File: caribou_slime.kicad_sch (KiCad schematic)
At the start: 30 parts, among them J1 BATT JST, Q1 AO3145, U1 ESP32-C3_SUPERMINI, U2 BMI270, U4 ME6211C33M5G, U5 FS312F-G, U6 FS8205A

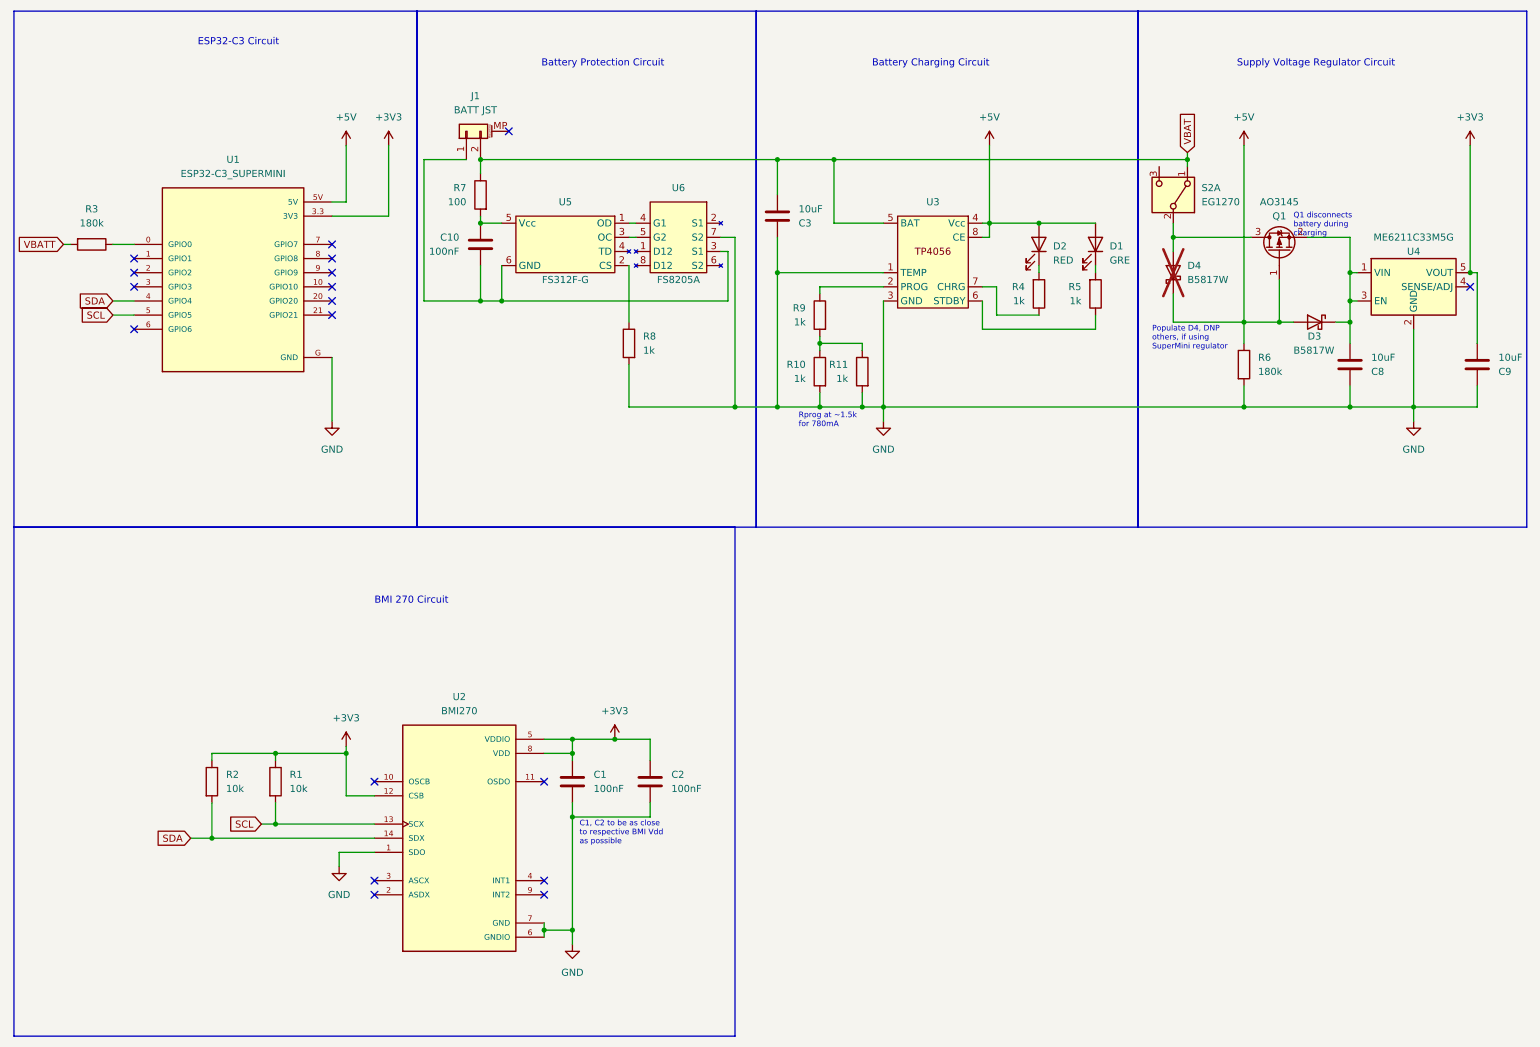
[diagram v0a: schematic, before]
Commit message: fix:(schematic): Create generic LED I limiting resistor array
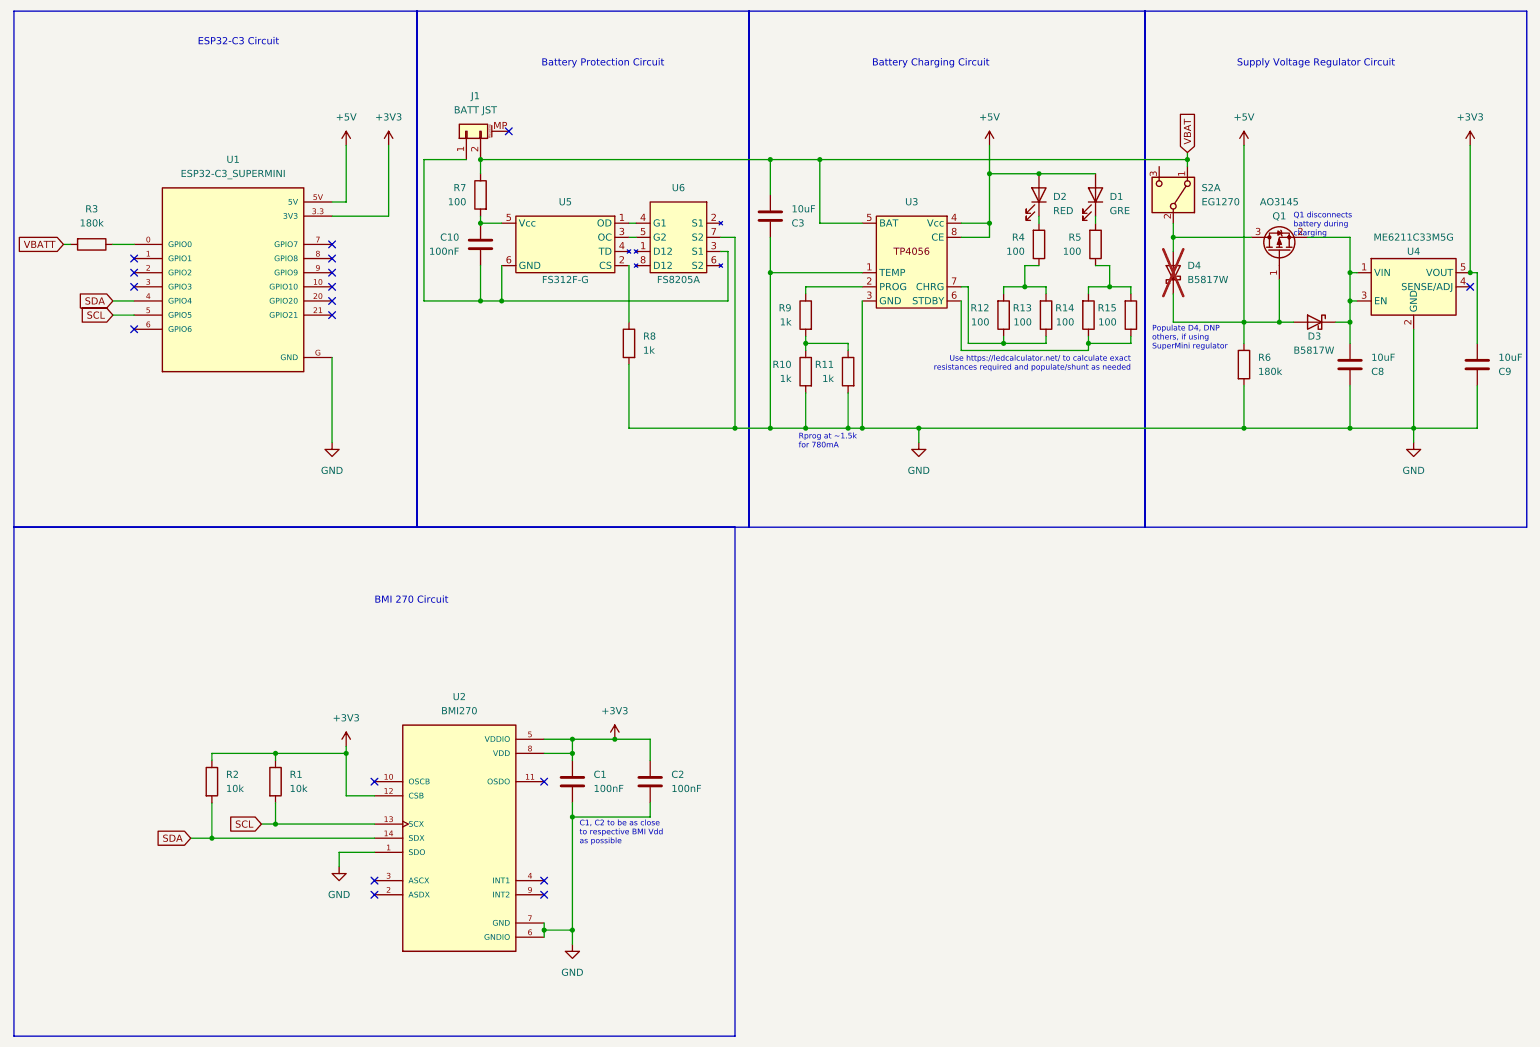
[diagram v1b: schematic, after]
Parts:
- added R12, R13, R14, R15: 100, Resistor_SMD:R_0805_2012Metric, symbol Device:R
- D1, D2: footprint (none) -> Diode_SMD:D_0805_2012Metric
- R4, R5: value 1k -> 100
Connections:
- net at R4.1: now also R12.2, R13.2; no longer U3.7 (CHRG)
- net at U3.6 (STDBY): now also R14.1, R15.1; no longer R5.1
- new net: R14.2, R15.2, R5.1
- new net: R12.1, R13.1, U3.7 (CHRG)
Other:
- note added: "Use https://ledcalculator.net/ to calculate exact resistances required and populate/shunt as needed"
- moved on the sheet: C3, D1, D2, R10, R11, R4, R5, R9, U3

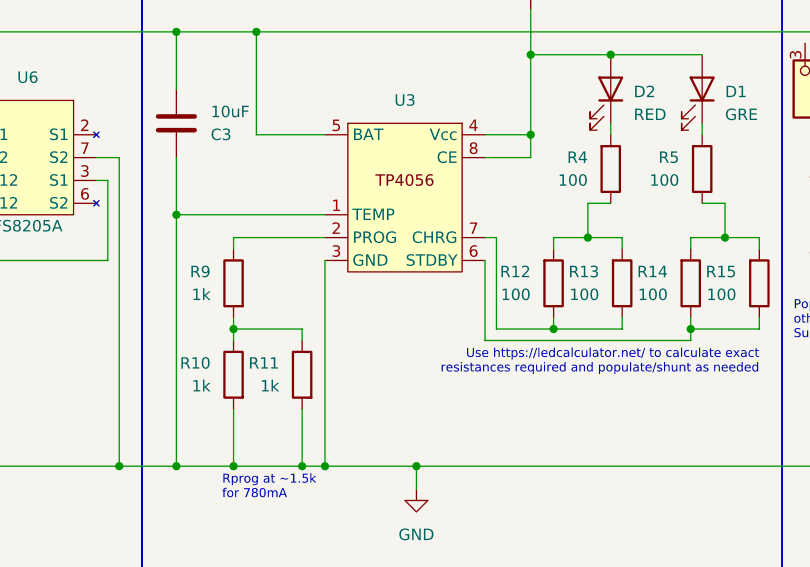
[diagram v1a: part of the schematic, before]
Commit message: chore(schematic): Link TP4056 datasheet and footprint
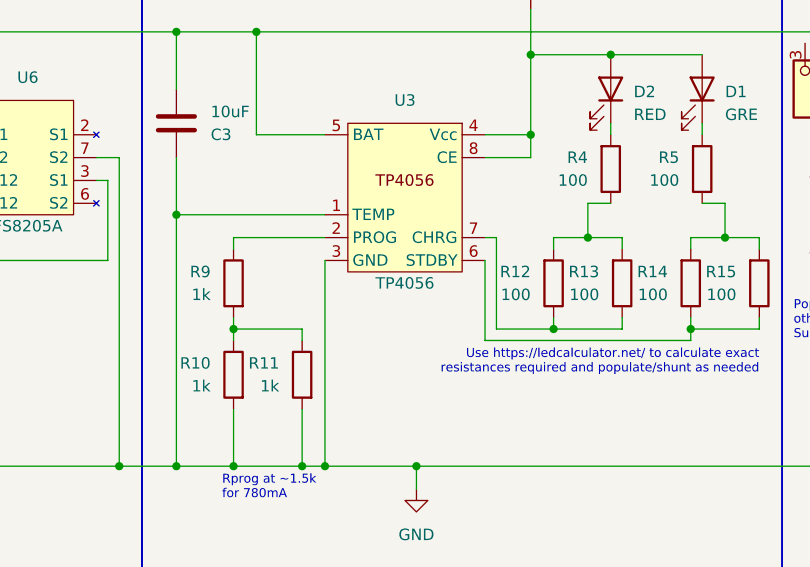
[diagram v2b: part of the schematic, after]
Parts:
- U3: value ~ -> TP4056; footprint (none) -> Package_SO:HSOP-8-1EP_3.9x4.9mm_P1.27mm_EP2.3x2.3mm
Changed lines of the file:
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@@
       (effects (font (size 1.27 1.27)))
     )
-    (property "Value" "~" (at 173.99 67.31 0)
+    (property "Value" "TP4056" (at 173.99 67.31 0)
       (effects (font (size 1.27 1.27)))
     )
-    (property "Footprint" "" (at 173.99 67.31 0)
+    (property "Footprint" "Package_SO:HSOP-8-1EP_3.9x4.9mm_P1.27mm_EP2.3x2.3mm" (at 173.99 67.31 0)
       (effects (font (size 1.27 1.27)) hide)
     )
-    (property "Datasheet" "" (at 173.99 67.31 0)
+    (property "Datasheet" "https://dlnmh9ip6v2uc.cloudfront.net/datasheets/Prototyping/TP4056.pdf" (at 173.99 67.31 0)
       (effects (font (size 1.27 1.27)) hide)
     )

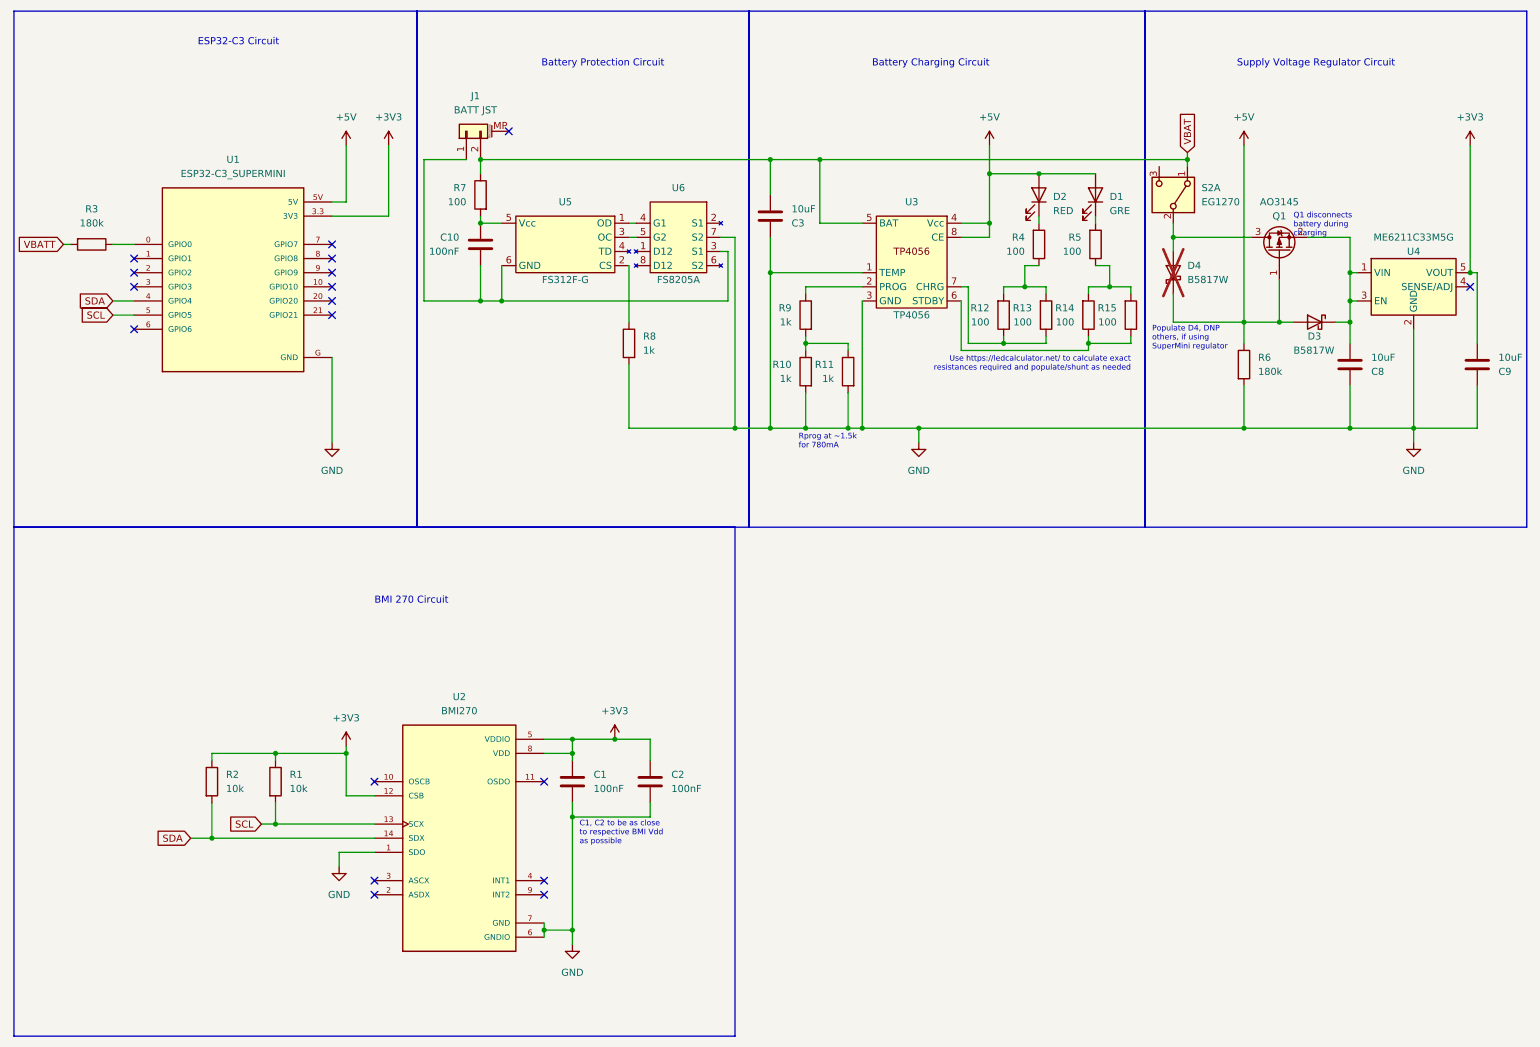
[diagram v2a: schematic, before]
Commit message: chore(schematic): Renumber schematic symbol reference designators
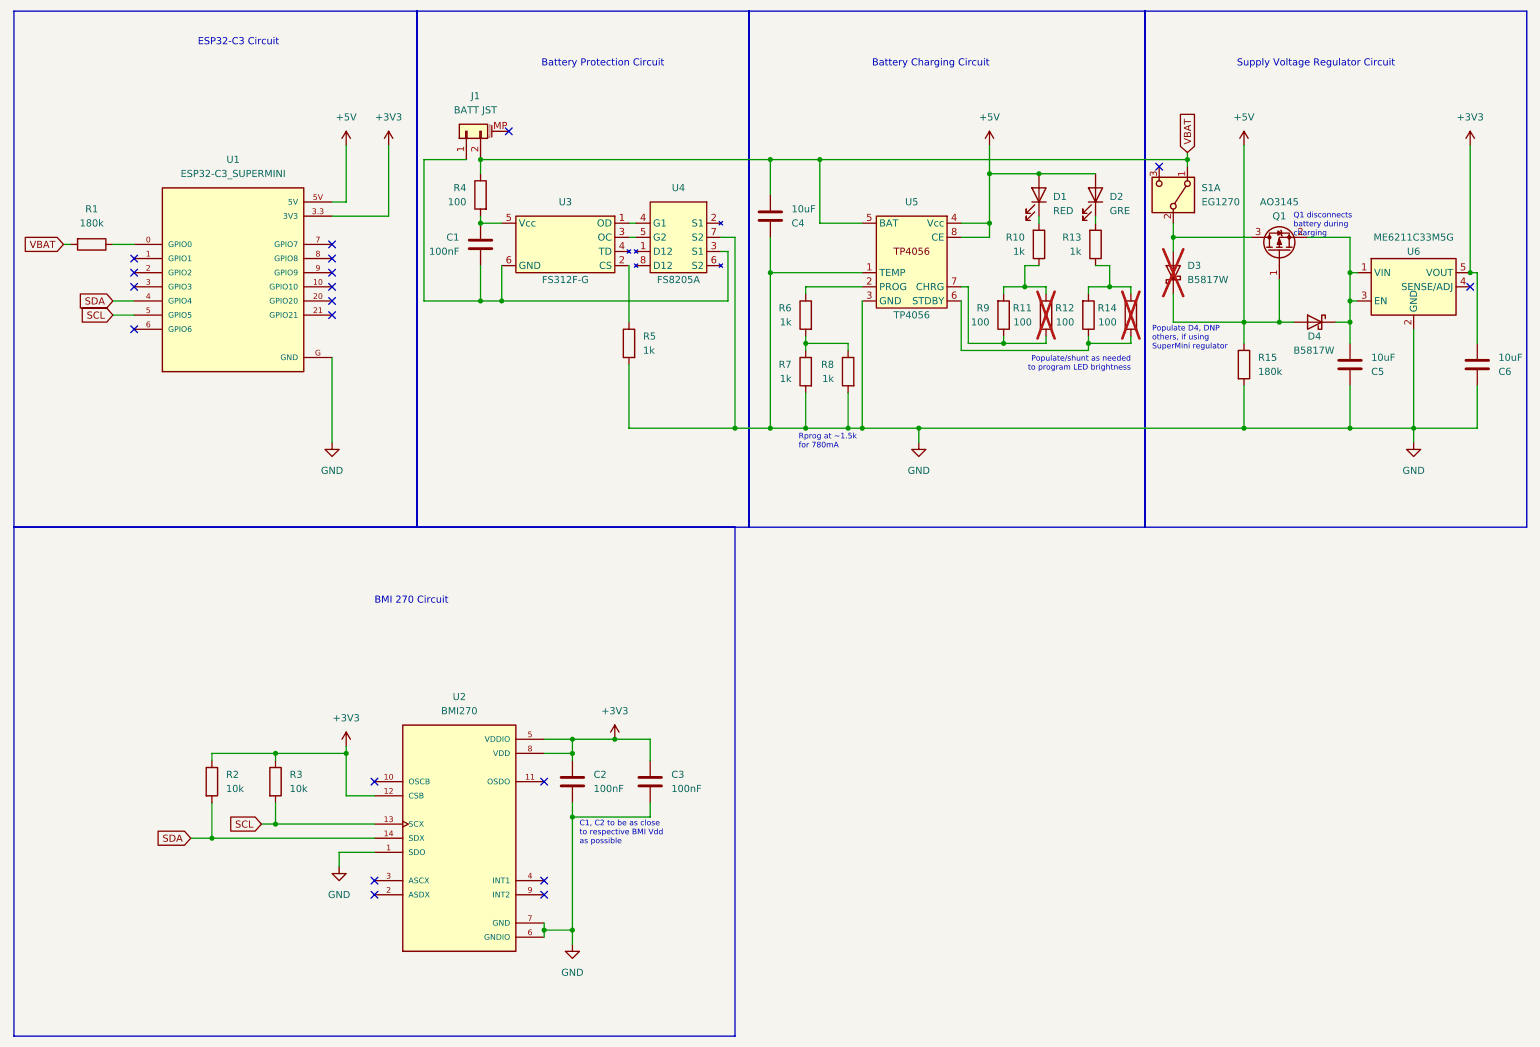
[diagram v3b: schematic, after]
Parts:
- C2: renamed from C1; footprint Connector_JST:JST_JWPF_B02B-JWPF-SK-R_1x02_P2.00mm_Vertical -> Capacitor_SMD:C_0805_2012Metric
- C4: renamed from C3; footprint Connector_JST:JST_JWPF_B02B-JWPF-SK-R_1x02_P2.00mm_Vertical -> Capacitor_SMD:C_0805_2012Metric
- C5: renamed from C8; footprint Connector_JST:JST_JWPF_B02B-JWPF-SK-R_1x02_P2.00mm_Vertical -> Capacitor_SMD:C_0805_2012Metric
- C6: renamed from C9; footprint Connector_JST:JST_JWPF_B02B-JWPF-SK-R_1x02_P2.00mm_Vertical -> Capacitor_SMD:C_0805_2012Metric
- R10: renamed from R4; value 100 -> 1k
- R11: renamed from R13; now not fitted
- R13: renamed from R5; value 100 -> 1k
- R14: renamed from R15; now not fitted
- renumbered C10 to C1, C2 to C3, D2 to D1, D1 to D2, D4 to D3, D3 to D4, R3 to R1, R14 to R12, R6 to R15, R1 to R3, R7 to R4, R8 to R5, R9 to R6, R10 to R7, R11 to R8, R12 to R9, S2 to S1, U5 to U3, U6 to U4, U3 to U5, U4 to U6
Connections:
- net VBATT is gone; now on net VBAT: R1.2
- no-connect marks 18 -> 19
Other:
- note added: "Populate/shunt as needed to program LED brightness"
- note removed: "Use https://ledcalculator.net/ to calculate exact resistances required and populate/shunt as needed"

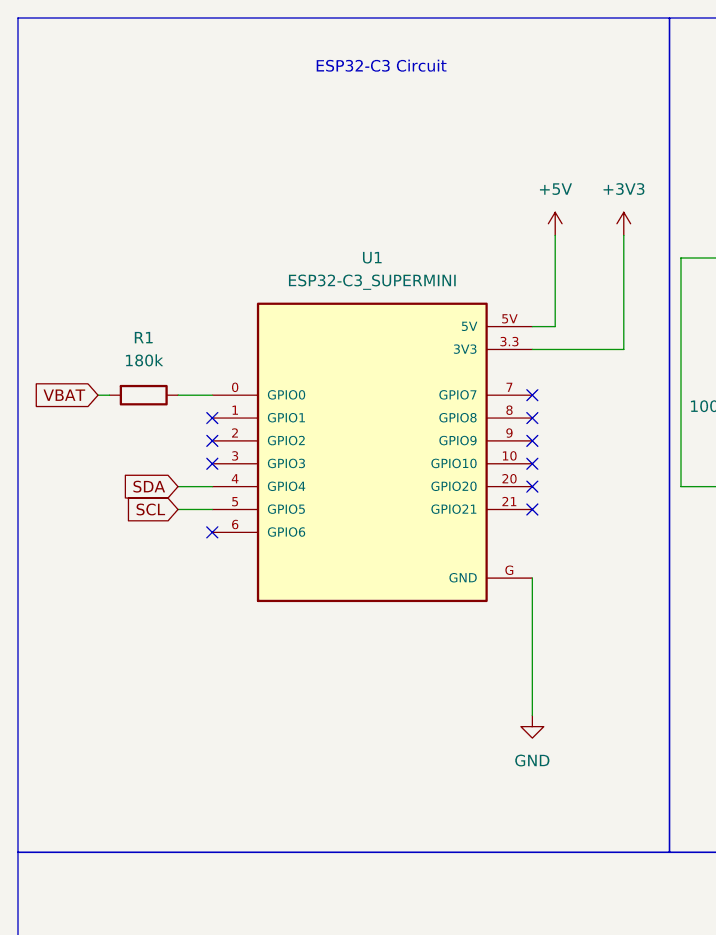
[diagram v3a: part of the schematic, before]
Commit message: fix(schematic): Add voltage divider to battery sense circuit
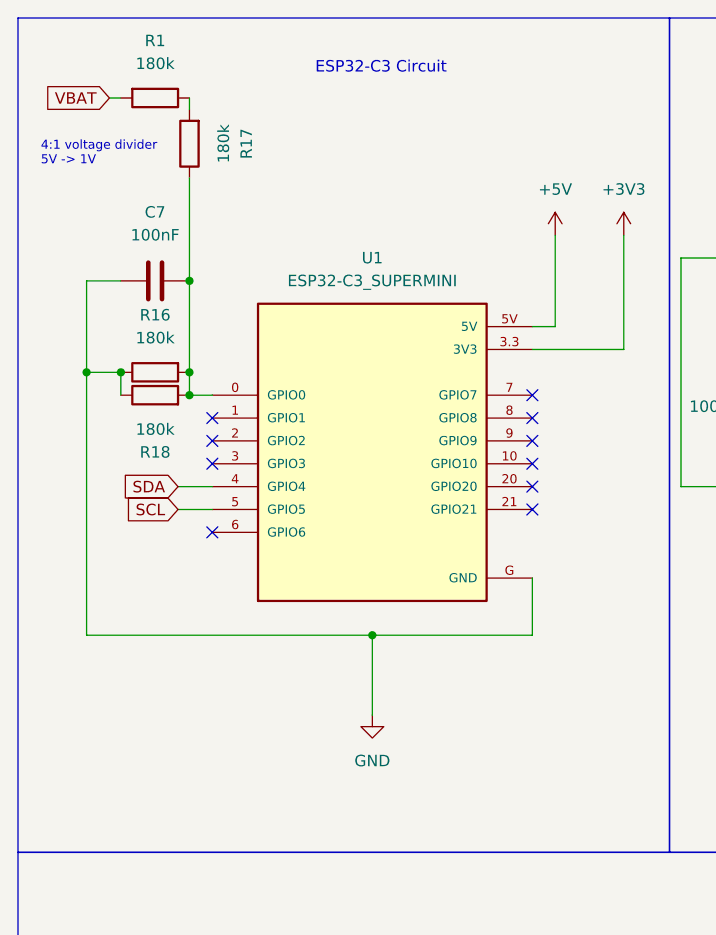
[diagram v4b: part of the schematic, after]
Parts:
- added C7: 100nF, Capacitor_SMD:C_0805_2012Metric, symbol Device:C
- added R16, R17, R18: 180k, Resistor_SMD:R_0805_2012Metric, symbol Device:R
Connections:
- net GND: now also C7.1, R16.1, R18.1
- net at R1.1: now also R17.2; no longer U1.0 (GPIO0)
- new net: C7.2, R16.2, R17.1, R18.2, U1.0 (GPIO0)
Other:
- note added: "4:1 voltage divider 5V -> 1V"
- moved on the sheet: R1
